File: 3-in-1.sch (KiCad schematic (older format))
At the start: 41 parts

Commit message: Layout cleanup
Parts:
- H1, H2: footprint MountingHole:MountingHole_2.7mm_M2.5 -> MountingHole:MountingHole_2.7mm_M2.5_ISO7380_Pad
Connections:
- net GND: now also H1.1, H2.1
- no-connect marks 64 -> 62
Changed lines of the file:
@@
 F 0 "H1" V 15554 6750 50  0000 L CNN
 F 1 "MountingHole" V 15645 6750 50  0000 L CNN
-F 2 "MountingHole:MountingHole_2.7mm_M2.5" H 15600 6600 50  0001 C CNN
+F 2 "MountingHole:MountingHole_2.7mm_M2.5_ISO7380_Pad" H 15600 6600 50  0001 C CNN
 F 3 "~" H 15600 6600 50  0001 C CNN
 	1    15600 6600
@@
 F 0 "H2" V 15554 7050 50  0000 L CNN
 F 1 "MountingHole" V 15645 7050 50  0000 L CNN
-F 2 "MountingHole:MountingHole_2.7mm_M2.5" H 15600 6900 50  0001 C CNN
+F 2 "MountingHole:MountingHole_2.7mm_M2.5_ISO7380_Pad" H 15600 6900 50  0001 C CNN
 F 3 "~" H 15600 6900 50  0001 C CNN
 	1    15600 6900
 	0    1    1    0
 $EndComp
-NoConn ~ 15500 6600
-NoConn ~ 15500 6900
 $Comp
 L Jumper:Jumper_2_Open ROM-JP1
@@
 Wire Wire Line
 	9900 9450 9800 9450
+$Comp
+L power:GND #PWR?
+U 1 1 5DD6E476
+P 15500 7150
+F 0 "#PWR?" H 15500 6900 50  0001 C CNN
+F 1 "GND" H 15505 6977 50  0000 C CNN
+F 2 "" H 15500 7150 50  0001 C CNN
+F 3 "" H 15500 7150 50  0001 C CNN
+	1    15500 7150
+	1    0    0    -1
+$EndComp
+Wire Wire Line
+	15500 7150 15500 6900
+Connection ~ 15500 6900
+Wire Wire Line
+	15500 6900 15500 6600
 $EndSCHEMATC

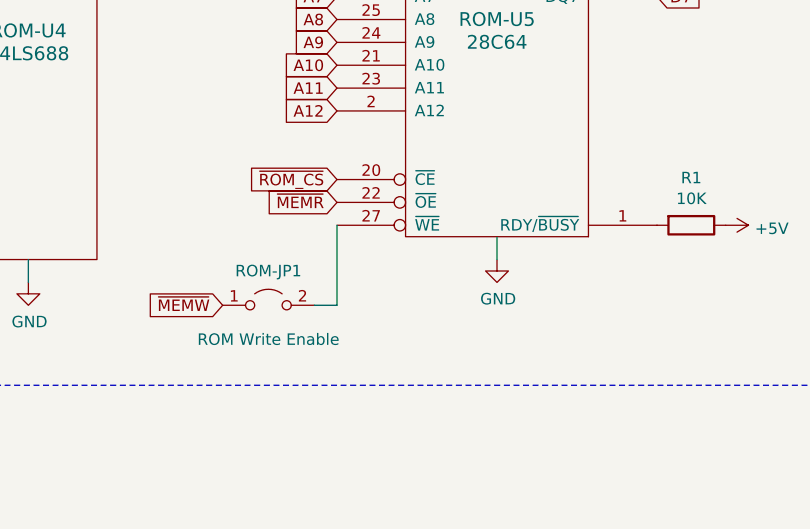
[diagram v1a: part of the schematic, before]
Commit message: Pull-up Resistor added
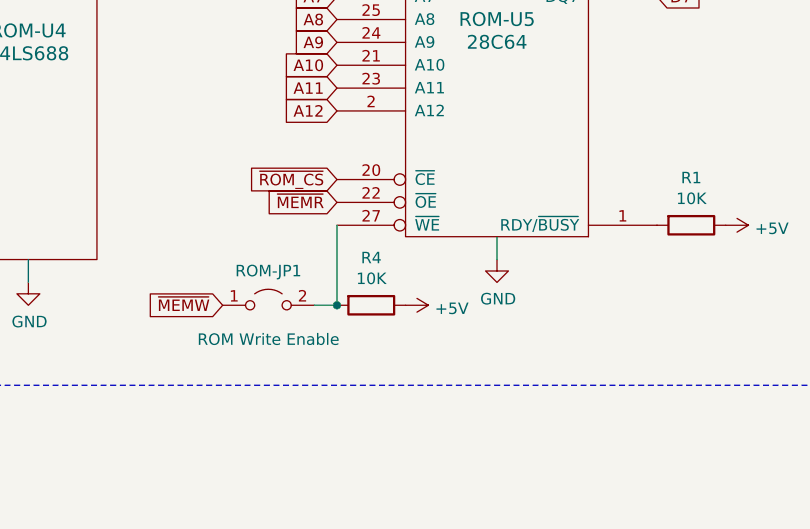
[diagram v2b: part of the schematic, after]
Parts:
- added R4: 10K, Resistor_THT:R_Axial_DIN0204_L3.6mm_D1.6mm_P5.08mm_Horizontal, symbol Device:R
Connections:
- net +5V: now also R4.1
- net at ROM-JP1.2 (B), ROM-U5.27 (~WE): now also R4.2
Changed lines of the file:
@@
 	9900 9450 9800 9450
 $Comp
-L power:GND #PWR?
+L power:GND #PWR0160
 U 1 1 5DD6E476
 P 15500 7150
-F 0 "#PWR?" H 15500 6900 50  0001 C CNN
+F 0 "#PWR0160" H 15500 6900 50  0001 C CNN
 F 1 "GND" H 15505 6977 50  0000 C CNN
 F 2 "" H 15500 7150 50  0001 C CNN
@@
 Wire Wire Line
 	15500 6900 15500 6600
+$Comp
+L Device:R R4
+U 1 1 5DE51C47
+P 10050 9450
+F 0 "R4" V 9843 9450 50  0000 C CNN
+F 1 "10K" V 9934 9450 50  0000 C CNN
+F 2 "Resistor_THT:R_Axial_DIN0204_L3.6mm_D1.6mm_P5.08mm_Horizontal" V 9980 9450 50  0001 C CNN
+F 3 "~" H 10050 9450 50  0001 C CNN
+	1    10050 9450
+	0    1    1    0
+$EndComp
+Connection ~ 9900 9450
+$Comp
+L power:+5V #PWR0161
+U 1 1 5DE52074
+P 10200 9450
+F 0 "#PWR0161" H 10200 9300 50  0001 C CNN
+F 1 "+5V" V 10215 9578 50  0000 L CNN
+F 2 "" H 10200 9450 50  0001 C CNN
+F 3 "" H 10200 9450 50  0001 C CNN
+	1    10200 9450
+	0    1    1    0
+$EndComp
 $EndSCHEMATC
